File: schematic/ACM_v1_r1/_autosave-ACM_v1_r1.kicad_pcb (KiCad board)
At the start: 4 copper layers, 25.5 x 39.9 mm, 34 parts, among them J1 DF40C-60DS-0.4V(51), J2 DF40C-60DS-0.4V(51), J3 Conn_02x04_Odd_Even, J4 Conn_01x02, J5 DF40C-60DS-0.4V(51), J6 DF40C-60DS-0.4V(51)

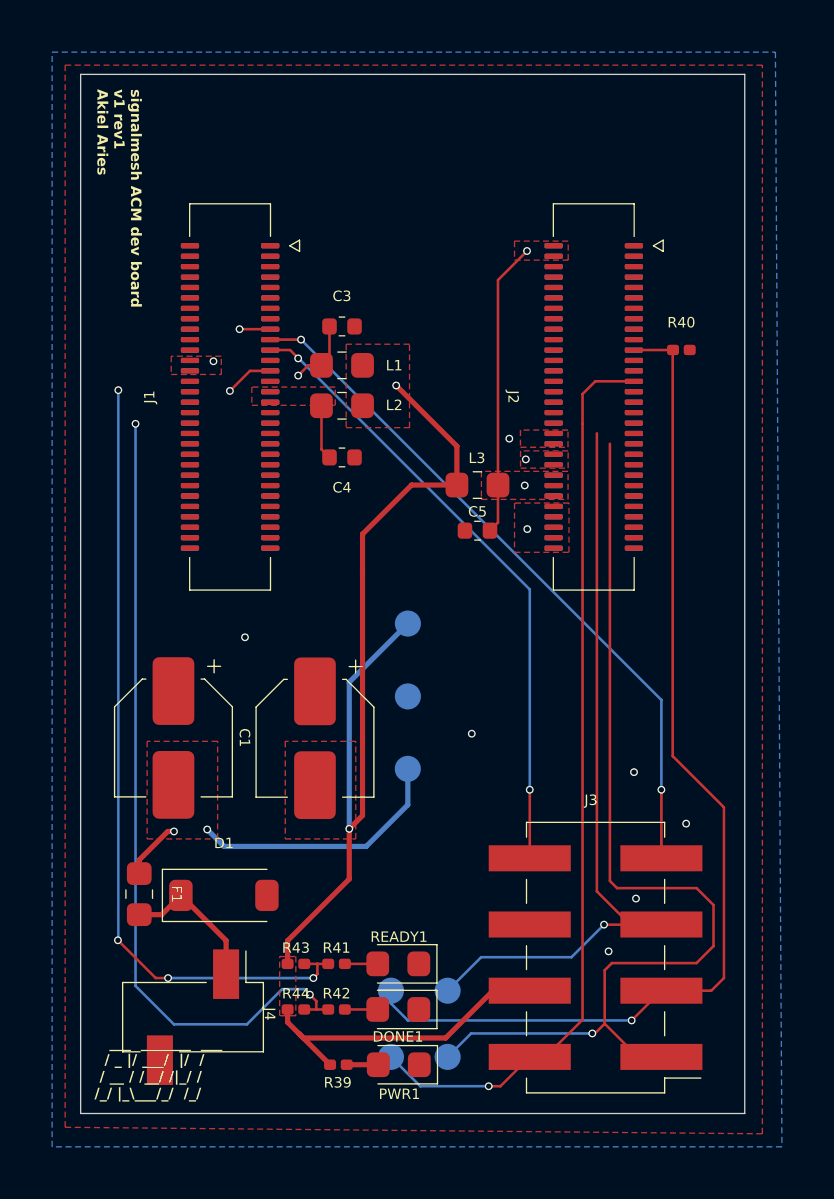
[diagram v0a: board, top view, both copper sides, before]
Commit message: add backside connector. fix front connector orientation
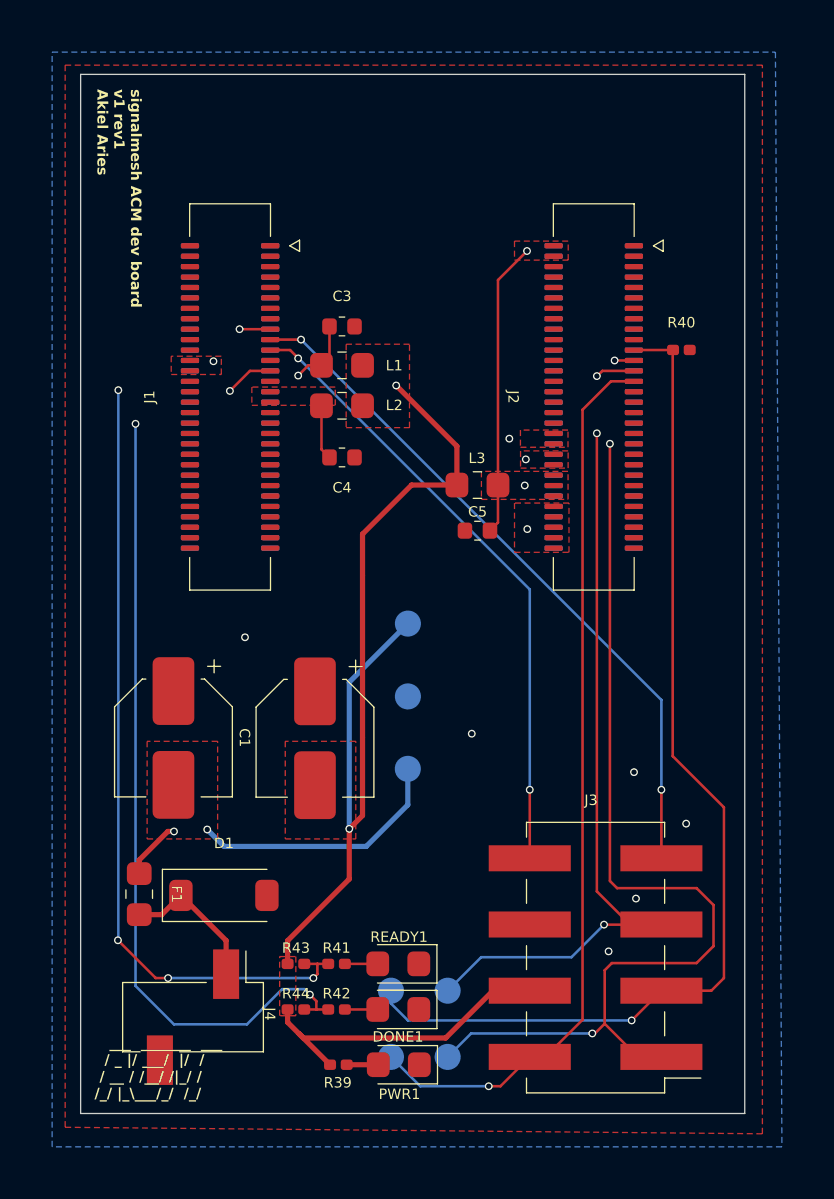
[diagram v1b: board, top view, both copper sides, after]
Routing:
- net /B1_JTAG_TMS: track 38.6 -> 42.6 mm, vias 1 -> 3
- net /A2_JTAG_TDO: track 29.8 -> 33.5 mm, vias 1 -> 3
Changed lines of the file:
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@@
 	)
 	(segment
-		(start 149.35 125.375)
-		(end 149.35 102.5)
+		(start 151.32 100.88)
+		(end 150.44 100.88)
+		(width 0.1)
+		(layer "F.Cu")
+		(net "/A3_JTAG_TDI")
+	)
+	(segment
+		(start 150.44 100.88)
+		(end 149.35 101.97)
 		(width 0.1)
 		(layer "F.Cu")
@@
 	)
 	(segment
-		(start 149.35 101.37)
-		(end 149.35 102.5)
-		(width 0.1)
-		(layer "F.Cu")
-		(net "/A3_JTAG_TDI")
-	)
-	(segment
-		(start 147.325 126.8)
+		(start 147.925 126.8)
+		(end 147.325 126.8)
+		(width 0.1)
+		(layer "F.Cu")
+		(net "/A3_JTAG_TDI")
+	)
+	(segment
+		(start 149.35 125.375)
 		(end 147.925 126.8)
 		(width 0.1)
@@
 	)
 	(segment
-		(start 147.925 126.8)
+		(start 149.35 101.97)
 		(end 149.35 125.375)
-		(width 0.1)
-		(layer "F.Cu")
-		(net "/A3_JTAG_TDI")
-	)
-	(segment
-		(start 151.32 100.88)
-		(end 149.84 100.88)
-		(width 0.1)
-		(layer "F.Cu")
-		(net "/A3_JTAG_TDI")
-	)
-	(segment
-		(start 149.84 100.88)
-		(end 149.35 101.37)
 		(width 0.1)
 		(layer "F.Cu")
@@
 	)
 	(segment
+		(start 151.32 100.08)
+		(end 150.58 100.08)
+		(width 0.1)
+		(layer "F.Cu")
+		(net "/B1_JTAG_TMS")
+	)
+	(segment
 		(start 150.2 125.525)
 		(end 150.2 123.475)
@@
 		(net "/B1_JTAG_TMS")
 	)
+	(via
+		(at 150.58 100.08)
+		(size 0.3)
+		(drill 0.2)
+		(layers "F.Cu" "B.Cu")
+		(net "/B1_JTAG_TMS")
+	)
+	(via
+		(at 150.4 103.275)
+		(size 0.3)
+		(drill 0.2)
+		(layers "F.Cu" "B.Cu")
+		(net "/B1_JTAG_TMS")
+	)
 	(segment
 		(start 144.175 126.8)
@@
 	)
 	(segment
+		(start 150.4 100.26)
+		(end 150.4 103.275)
+		(width 0.1)
+		(layer "In2.Cu")
+		(net "/B1_JTAG_TMS")
+	)
+	(segment
+		(start 150.58 100.08)
+		(end 150.4 100.26)
+		(width 0.1)
+		(layer "In2.Cu")
+		(net "/B1_JTAG_TMS")
+	)
+	(segment
+		(start 150.11 100.48)
+		(end 151.32 100.48)
+		(width 0.1)
+		(layer "F.Cu")
+		(net "/A2_JTAG_TDO")
+	)
+	(segment
+		(start 149.9 100.68)
+		(end 149.91 100.68)
+		(width 0.1)
+		(layer "F.Cu")
+		(net "/A2_JTAG_TDO")
+	)
+	(segment
 		(start 149.9 120.45)
 		(end 149.9 102.875)
@@
 	)
 	(segment
+		(start 149.91 100.68)
+		(end 150.11 100.48)
+		(width 0.1)
+		(layer "F.Cu")
+		(net "/A2_JTAG_TDO")
+	)
+	(segment
 		(start 150.175 121.725)
 		(end 152.37 121.725)
@@
 	)
 	(via
+		(at 149.9 100.68)
+		(size 0.3)
+		(drill 0.2)
+		(layers "F.Cu" "B.Cu")
+		(net "/A2_JTAG_TDO")
+	)
+	(via
 		(at 150.175 121.725)
+		(size 0.3)
+		(drill 0.2)
+		(layers "F.Cu" "B.Cu")
+		(net "/A2_JTAG_TDO")
+	)
+	(via
+		(at 149.9 102.875)
 		(size 0.3)
 		(drill 0.2)
@@
 		(net "/A2_JTAG_TDO")
 	)
+	(segment
+		(start 149.9 102.875)
+		(end 149.9 100.68)
+		(width 0.1)
+		(layer "In2.Cu")
+		(net "/A2_JTAG_TDO")
+	)
